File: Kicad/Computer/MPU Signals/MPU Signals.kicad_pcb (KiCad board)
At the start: 2 copper layers, 61 x 127 mm, 35 parts, among them IC1 FAN2558S38X, IC2 W65C816S6TQG-14, IC3 74LVC573AD,112, IC4 74LVC4245APW,118, IC5 74LVC04AD,118, IC6 74LVC32APW,118, IC7 74LVC1G08GV,125, IC8 74LVC11PW,112, J1 Conn_01x02_Male, J10 Conn_01x02_Male, J2 Conn_01x02_Male, J3 Conn_01x02_Male, J4 Conn_01x18_Male, J5 Conn_01x02_Male, J6 Conn_01x02_Male, J7 Conn_01x32_Male, J8 Conn_01x02_Male, J9 Conn_01x02_Male

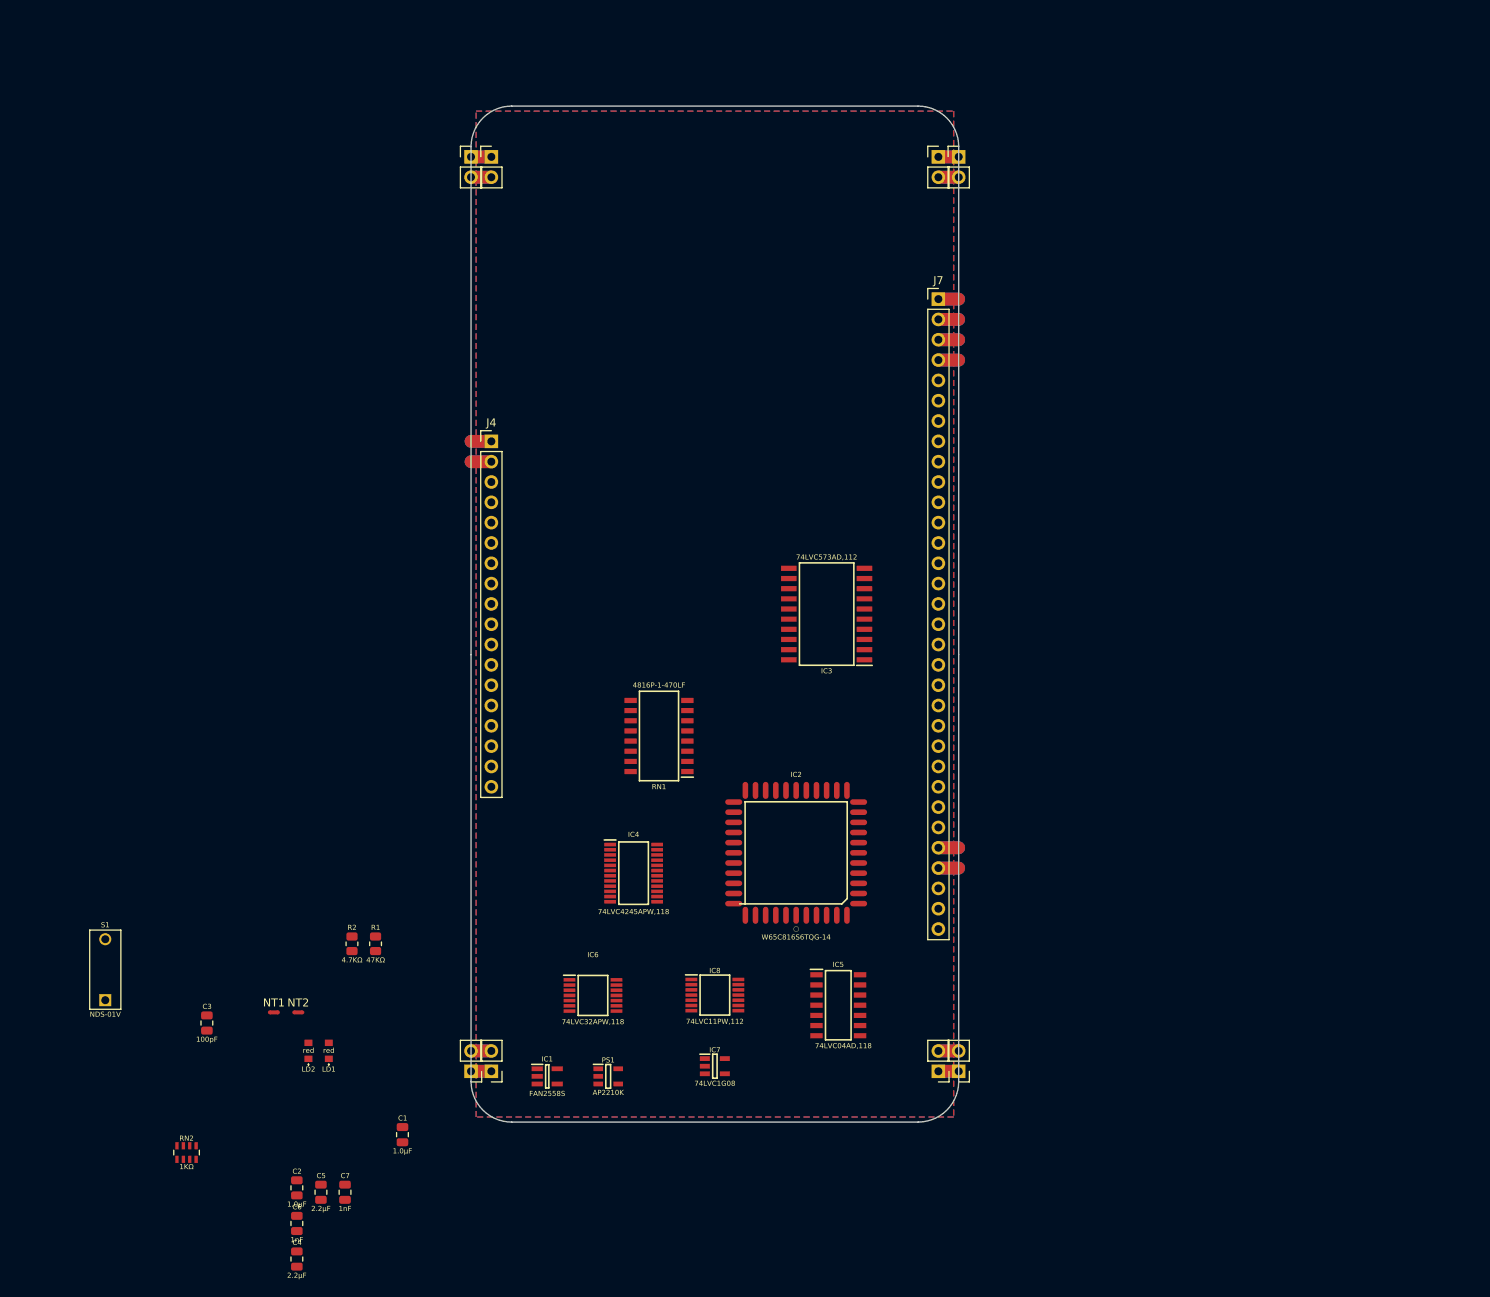
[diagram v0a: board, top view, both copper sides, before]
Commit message: Added Seven segment LED displays for CPU busses.
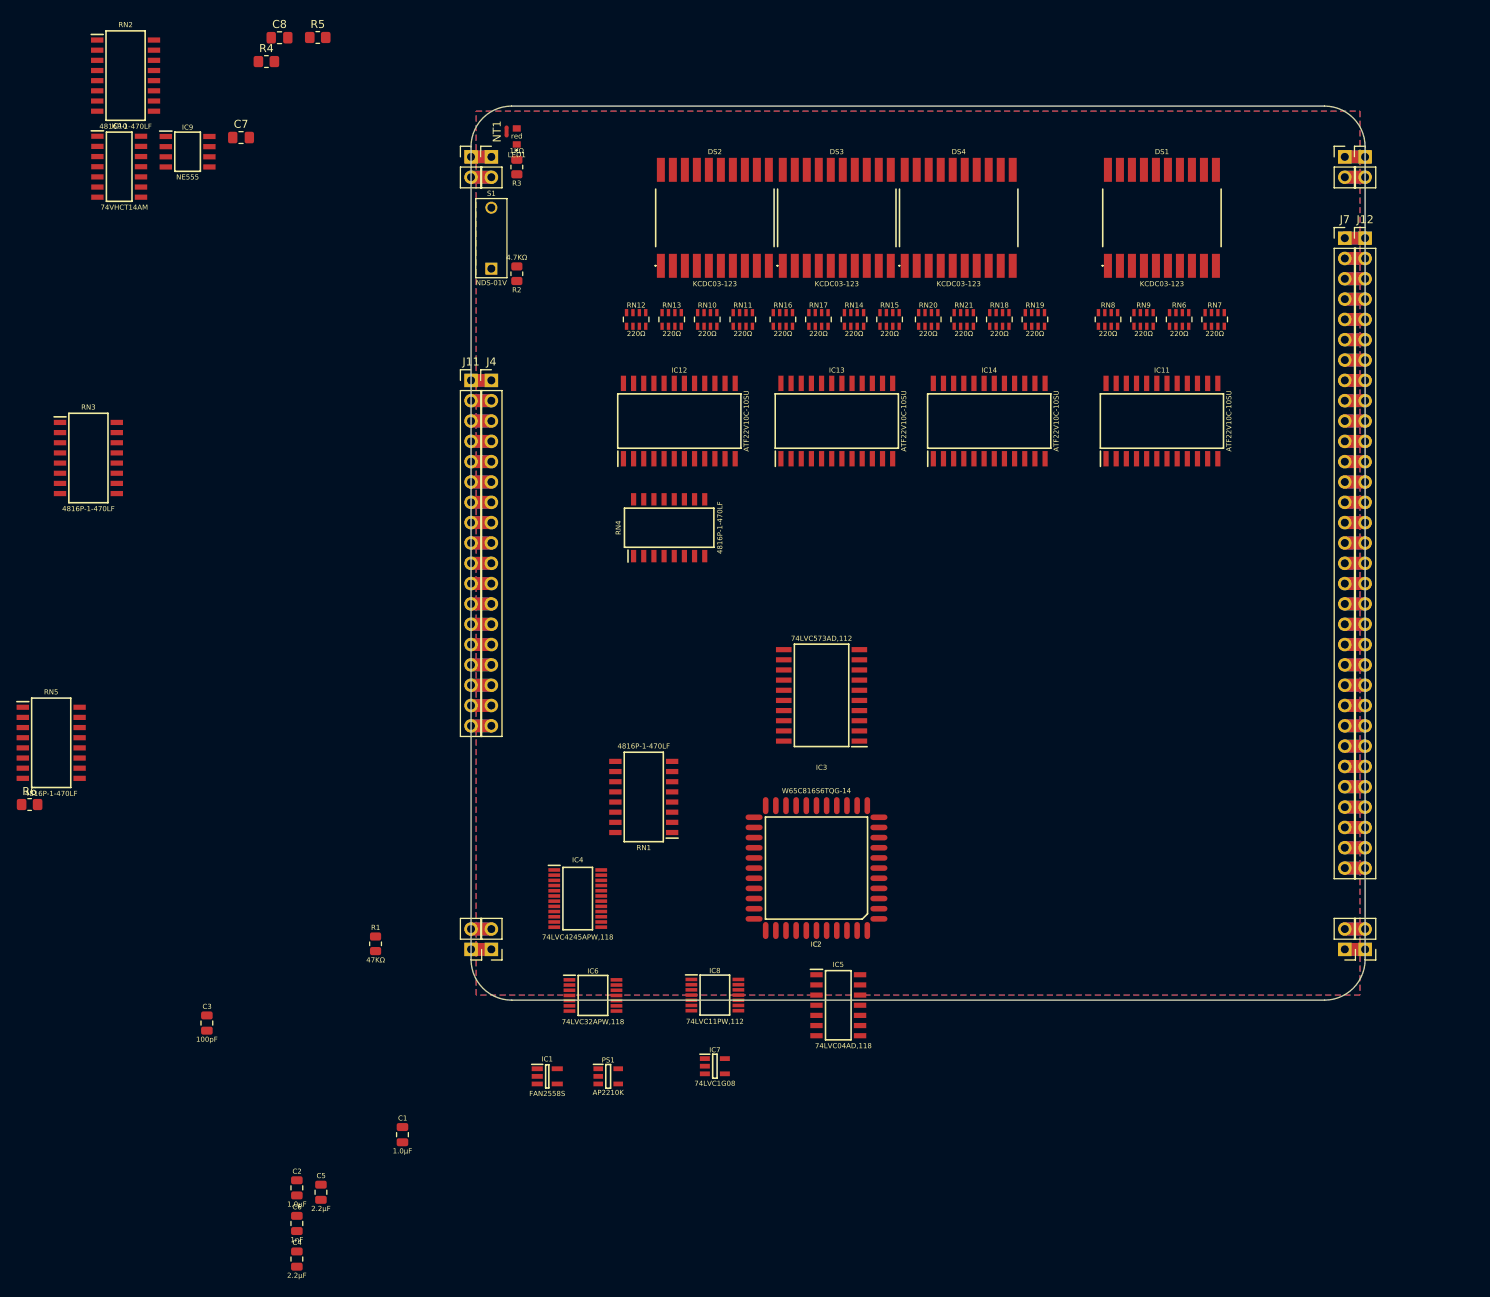
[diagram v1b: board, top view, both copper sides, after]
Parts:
- removed LD2: 150224SS73100, SamacSys_Parts:150224SS73100A
- removed NT2: NetTie_2, NetTie:NetTie-2_SMD_Pad0.5mm
- added C8: C_Small, Capacitor_SMD:C_0805_2012Metric_Pad1.18x1.45mm_HandSolder, F.Cu at (39.6, 41.0)
- added DS1: KCDC03-123, SamacSys_Parts:KCDC03123, F.Cu at (149.9, 63.5)
- added DS2: KCDC03-123, SamacSys_Parts:KCDC03123, F.Cu at (94.0, 63.5)
- added DS3: KCDC03-123, SamacSys_Parts:KCDC03123, F.Cu at (109.2, 63.5)
- added DS4: KCDC03-123, SamacSys_Parts:KCDC03123, F.Cu at (124.5, 63.5)
- added IC10: 74VHCT14AM, SamacSys_Parts:SOIC127P600X175-14N, F.Cu at (19.5, 57.1)
- added IC11: ATF22V10C-10SU, SamacSys_Parts:SOIC127P1032X265-24N, F.Cu at (149.9, 88.9)
- added IC12: ATF22V10C-10SU, SamacSys_Parts:SOIC127P1032X265-24N, F.Cu at (89.5, 88.9)
- added IC13: ATF22V10C-10SU, SamacSys_Parts:SOIC127P1032X265-24N, F.Cu at (109.2, 88.9)
- added IC14: ATF22V10C-10SU, SamacSys_Parts:SOIC127P1032X265-24N, F.Cu at (128.3, 88.9)
- added IC9: NE555DRG4, SamacSys_Parts:SOIC127P600X175-8N, F.Cu at (28.1, 55.2)
- added J11: Conn_01x18_Male, Connector_PinHeader_2.54mm:PinHeader_1x18_P2.54mm_Vertical, F.Cu at (63.5, 83.8)
- added J12: Conn_01x32_Male, Connector_PinHeader_2.54mm:PinHeader_1x32_P2.54mm_Vertical, F.Cu at (175.3, 66.0)
- added R3: R_0805, SamacSys_Parts:R_0805, F.Cu at (69.2, 57.1)
- added R4: R_Small, Resistor_SMD:R_0805_2012Metric_Pad1.20x1.40mm_HandSolder, F.Cu at (37.9, 44.0)
- added R5: R_Small, Resistor_SMD:R_0805_2012Metric_Pad1.20x1.40mm_HandSolder, F.Cu at (44.3, 41.0)
- added R6: R_Small, Resistor_SMD:R_0805_2012Metric_Pad1.20x1.40mm_HandSolder, F.Cu at (8.32, 136.8)
- added RN10: CAY16-221J4LF, SamacSys_Parts:CAY1647R0F4LF, F.Cu at (93.0, 76.2)
- added RN11: CAY16-221J4LF, SamacSys_Parts:CAY1647R0F4LF, F.Cu at (97.5, 76.2)
- added RN12: CAY16-221J4LF, SamacSys_Parts:CAY1647R0F4LF, F.Cu at (84.1, 76.2)
- added RN13: CAY16-221J4LF, SamacSys_Parts:CAY1647R0F4LF, F.Cu at (88.6, 76.2)
- added RN14: CAY16-221J4LF, SamacSys_Parts:CAY1647R0F4LF, F.Cu at (111.4, 76.2)
- added RN15: CAY16-221J4LF, SamacSys_Parts:CAY1647R0F4LF, F.Cu at (115.8, 76.2)
- added RN16: CAY16-221J4LF, SamacSys_Parts:CAY1647R0F4LF, F.Cu at (102.5, 76.2)
- added RN17: CAY16-221J4LF, SamacSys_Parts:CAY1647R0F4LF, F.Cu at (106.9, 76.2)
- added RN18: CAY16-221J4LF, SamacSys_Parts:CAY1647R0F4LF, F.Cu at (129.5, 76.2)
- added RN19: CAY16-221J4LF, SamacSys_Parts:CAY1647R0F4LF, F.Cu at (134.0, 76.2)
- added RN20: CAY16-221J4LF, SamacSys_Parts:CAY1647R0F4LF, F.Cu at (120.7, 76.2)
- added RN21: CAY16-221J4LF, SamacSys_Parts:CAY1647R0F4LF, F.Cu at (125.1, 76.2)
- added RN3: 4816P-1-470LF, SamacSys_Parts:SOIC127P762X240-16N, F.Cu at (15.7, 93.5)
- added RN4: 4816P-1-470LF, SamacSys_Parts:SOIC127P762X240-16N, F.Cu at (88.3, 102.2)
- added RN5: 4816P-1-470LF, SamacSys_Parts:SOIC127P762X240-16N, F.Cu at (11.0, 129.1)
- added RN6: CAY16-221J4LF, SamacSys_Parts:CAY1647R0F4LF, F.Cu at (152.0, 76.2)
- added RN7: CAY16-221J4LF, SamacSys_Parts:CAY1647R0F4LF, F.Cu at (156.5, 76.2)
- added RN8: CAY16-221J4LF, SamacSys_Parts:CAY1647R0F4LF, F.Cu at (143.1, 76.2)
- added RN9: CAY16-221J4LF, SamacSys_Parts:CAY1647R0F4LF, F.Cu at (147.6, 76.2)
- C7: value C_0805 -> C_Small; footprint SamacSys_Parts:C_0805 -> Capacitor_SMD:C_0805_2012Metric_Pad1.18x1.45mm_HandSolder
- RN2: value CAY16-102J4LF -> 4816P-1-470LF; footprint SamacSys_Parts:CAY16-J4 -> SamacSys_Parts:SOIC127P762X240-16N
- moved RN2 134.8 mm to (20.3, 45.7)
- moved C7 132.5 mm to (34.8, 53.5)
- moved LED1 116.7 mm to (69.2, 53.3)
- moved NT1 113.9 mm to (67.9, 52.7), turned to 90 degrees
- moved S1 103.4 mm to (66.0, 69.8)
- moved R2 86.3 mm to (69.2, 70.5), turned to 180 degrees
- moved J10 53.0 mm to (175.3, 154.9)
- moved J8 53.0 mm to (172.7, 154.9)
- moved J7 51.4 mm to (172.7, 66.0)
- moved J6 50.8 mm to (172.7, 55.9)
- moved J9 50.8 mm to (175.3, 55.9)
- moved J2 15.2 mm to (63.5, 154.9)
- moved J5 15.2 mm to (66.0, 154.9)
- moved IC3 10.2 mm to (107.3, 123.2)
- moved RN1 7.85 mm to (85.1, 135.9)
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- renumbered LD1 to LED1
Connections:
- net /LED Enable renamed /~{LED Enable}
- C7 pad 1: /5V -> Net-(C7-Pad1)
- IC4 pad 1: /5V -> unconnected-(IC4-Pad1)
- LED1 pad 1: Net-(LD1-Pad1) -> Net-(LED1-Pad1)
- RN2 pad 1: GND -> /A0
- RN2 pad 2: unconnected-(RN2-Pad2) -> /A1
- RN2 pad 3: unconnected-(RN2-Pad3) -> /A2
- RN2 pad 4: GND -> /A3
- RN2 pad 5: Net-(LD2-Pad1) -> /A4
- RN2 pad 6: unconnected-(RN2-Pad6) -> /A5
- RN2 pad 7: unconnected-(RN2-Pad7) -> /A6
- RN2 pad 8: Net-(LD1-Pad1) -> /A7
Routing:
- net /~{NMI}: track 0.00 -> 5.08 mm
- net /~{IRQ}: track 0.00 -> 5.08 mm
- net /~{Data Transmit}: track 0.00 -> 5.08 mm
- net /~{Clock Enable}: track 0.00 -> 5.08 mm
- net /Write Selector: track 0.00 -> 5.08 mm
- net /Read Selector: track 0.00 -> 5.08 mm
- net /RDY: track 0.00 -> 5.08 mm
- net /D7: track 0.00 -> 5.08 mm
- net /D6: track 0.00 -> 5.08 mm
- net /D5: track 0.00 -> 5.08 mm
- net /D4: track 0.00 -> 5.08 mm
- net /D3: track 0.00 -> 5.08 mm
- net /D2: track 0.00 -> 5.08 mm
- net /D1: track 0.00 -> 5.08 mm
- net /D0: track 0.00 -> 5.08 mm
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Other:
- board size 61 x 127 mm -> 111.8 x 111.8 mm

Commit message: MPU Signals.
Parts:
- removed RN2, RN4: 4816P-1-470LF, SamacSys_Parts:SOIC127P762X240-16N
- added J13: Conn_01x08_Male, Connector_PinHeader_2.54mm:PinHeader_1x12_P2.54mm_Vertical, B.Cu at (143.5, 77.5)
- added J14: Conn_01x12_Male, Connector_PinHeader_2.54mm:PinHeader_1x12_P2.54mm_Vertical, B.Cu at (143.5, 74.9)
- added J15: Conn_01x16_Male, Connector_PinHeader_2.54mm:PinHeader_1x12_P2.54mm_Vertical, B.Cu at (143.5, 133.3)
- added J16: Conn_01x12_Male, Connector_PinHeader_2.54mm:PinHeader_1x12_P2.54mm_Vertical, B.Cu at (143.5, 135.9)
- added J17: Conn_02x05_Counter_Clockwise, SamacSys_Parts:Pin_Socket_1.27mm 2x05, F.Cu at (135.9, 78.7)
- added J18: Conn_02x05_Counter_Clockwise, SamacSys_Parts:Pin_Header_1.27mm 2x05, B.Cu at (68.6, 78.7)
- added J19: SamacSys_Parts:Pin_Header_1.27mm 2x05, SamacSys_Parts:Pin_Header_1.27mm 2x05, B.Cu at (68.6, 130.8)
- added J20: Conn_02x05_Counter_Clockwise, SamacSys_Parts:Pin_Socket_1.27mm 2x05, F.Cu at (135.9, 130.8)
- added J21: SamacSys_Parts:Pin_Header_1.27mm 2x05, SamacSys_Parts:Pin_Header_1.27mm 2x05, B.Cu at (111.8, 78.7)
- added J22: Conn_02x05_Counter_Clockwise, SamacSys_Parts:Pin_Socket_1.27mm 2x05, F.Cu at (179.1, 78.7)
- added J23: SamacSys_Parts:Pin_Header_1.27mm 2x05, SamacSys_Parts:Pin_Header_1.27mm 2x05, B.Cu at (111.8, 130.8)
- added J24: Conn_02x05_Counter_Clockwise, SamacSys_Parts:Pin_Socket_1.27mm 2x05, F.Cu at (179.1, 130.8)
- C6, C7, C8, IC11, IC12, IC13, IC14, IC9, J1, J10, J2, J3, J5, J6, J8, J9, NT1, R3, R4, R5, R6: moved to B.Cu
- IC10: value 74VHCT14AM -> 74LVC1G17GV,125; footprint SamacSys_Parts:SOIC127P600X175-14N -> SamacSys_Parts:SOT95P275X110-5N; moved to B.Cu
- J11, J4: value Conn_01x18_Male -> Conn_01x10_Male; footprint Connector_PinHeader_2.54mm:PinHeader_1x18_P2.54mm_Vertical -> Connector_PinHeader_2.54mm:PinHeader_1x10_P2.54mm_Vertical; moved to B.Cu
- J12, J7: value Conn_01x32_Male -> Conn_01x16_Male; footprint Connector_PinHeader_2.54mm:PinHeader_1x32_P2.54mm_Vertical -> Connector_PinHeader_2.54mm:PinHeader_1x16_P2.54mm_Vertical; moved to B.Cu
- moved RN3 157.1 mm to (172.7, 95.2), turned to 90 degrees
- moved RN5 154.8 mm to (160.0, 87.0), turned to -90 degrees
- moved C4 151.9 mm to (147.3, 84.5), turned to 90 degrees
- moved C3 138.2 mm to (148.0, 91.4), turned to 90 degrees
- moved C5 137.7 mm to (138.4, 84.5), turned to 90 degrees
- moved C2 134.8 mm to (135.3, 87.6)
- moved C1 127.1 mm to (144.1, 87.6)
- moved C6 120.0 mm to (110.3, 90.8), turned to -90 degrees
- moved R6 107.8 mm to (101.1, 81.9)
- moved R1 107.2 mm to (138.4, 91.4), turned to 90 degrees
- moved PS1 107.0 mm to (148.0, 87.6)
- moved IC1 105.8 mm to (138.4, 87.6)
- moved IC10 95.5 mm to (110.0, 87.6)
- moved IC4 95.0 mm to (157.5, 98.4), turned to -90 degrees
- moved R4 87.0 mm to (113.2, 87.6), turned to 90 degrees
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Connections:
- net /Address High Display/Digit 0 C Seg renamed /High Address Display/Digit 0 C Seg
- net /Address High Display/Digit 0 D Seg renamed /High Address Display/Digit 0 D Seg
- net /Address High Display/Digit 0 E Seg renamed /High Address Display/Digit 0 E Seg
- net /Address High Display/Digit L0 Cathode renamed /High Address Display/Digit L0 Cathode
- net /Address High Display/Digit R0 Cathode renamed /High Address Display/Digit R0 Cathode
- net /Address Low Display/Digit 0 C Seg renamed /Low Address Display/Digit 0 C Seg
- net /Address Low Display/Digit 0 D Seg renamed /Low Address Display/Digit 0 D Seg
- net /Address Low Display/Digit 0 E Seg renamed /Low Address Display/Digit 0 E Seg
- net /Address Low Display/Digit L0 Cathode renamed /Low Address Display/Digit L0 Cathode
- net /Address Low Display/Digit R0 Cathode renamed /Low Address Display/Digit R0 Cathode
- net /BA Display/Digit 0 C Seg renamed /Bank Address Display/Digit 0 C Seg
- net /BA Display/Digit 0 D Seg renamed /Bank Address Display/Digit 0 D Seg
- net /BA Display/Digit 0 E Seg renamed /Bank Address Display/Digit 0 E Seg
- net /BA Display/Digit L0 Cathode renamed /Bank Address Display/Digit L0 Cathode
- net /BA Display/Digit R0 Cathode renamed /Bank Address Display/Digit R0 Cathode
- C6 pad 1: /5V -> /3.8V_{TOP}
- C6 pad 2: GND -> /GND_{TOP}
- C7 pad 2: GND -> /GND_{TOP}
- C8 pad 2: GND -> /GND_{TOP}
- DS1 pad 10: GND -> /GND_{TOP}
- DS1 pad 5: GND -> /GND_{TOP}
- DS2 pad 10: GND -> /GND_{TOP}
- DS2 pad 5: GND -> /GND_{TOP}
- DS3 pad 10: GND -> /GND_{TOP}
- DS3 pad 5: GND -> /GND_{TOP}
- DS4 pad 10: GND -> /GND_{TOP}
- DS4 pad 5: GND -> /GND_{TOP}
- IC10 pad 1: Net-(IC10-Pad1) -> unconnected-(IC10-Pad1)
- IC10 pad 2: GND -> Net-(IC10-Pad2)
- IC10 pad 3: Net-(IC10-Pad3) -> /GND_{TOP}
- IC10 pad 4: unconnected-(IC10-Pad4) -> Net-(IC10-Pad4)
- IC10 pad 5: Net-(IC10-Pad3) -> /3.8V_{TOP}
- IC11 pad 12: GND -> /GND_{TOP}
- IC11 pad 13: GND -> /GND_{TOP}
- IC11 pad 2: /LD0 -> /LD0_{TOP}
- IC11 pad 24: /5V -> /5V_{TOP}
- IC11 pad 3: /LD1 -> /LD1_{TOP}
- IC11 pad 4: /LD2 -> /LD2_{TOP}
- IC11 pad 5: /LD3 -> /LD3_{TOP}
- IC11 pad 6: /LD4 -> /LD4_{TOP}
- IC11 pad 7: /LD5 -> /LD5_{TOP}
- IC11 pad 8: /LD6 -> /LD6_{TOP}
- IC11 pad 9: /LD7 -> /LD7_{TOP}
- IC12 pad 12: GND -> /GND_{TOP}
- IC12 pad 13: GND -> /GND_{TOP}
- IC12 pad 16: /BA Display/Digit 0 B Seg -> /Bank Address Display/Digit 0 B Seg
- IC12 pad 17: /BA Display/Digit 0 A Seg -> /Bank Address Display/Digit 0 A Seg
- IC12 pad 19: /BA Display/Digit 0 F Seg -> /Bank Address Display/Digit 0 F Seg
- IC12 pad 2: /LBA0 -> /BA0_{TOP}
- IC12 pad 21: /BA Display/Digit 0 G Seg -> /Bank Address Display/Digit 0 G Seg
- IC12 pad 24: /5V -> /5V_{TOP}
- IC12 pad 3: /LBA1 -> /BA1_{TOP}
- IC12 pad 4: /LBA2 -> /BA2_{TOP}
- IC12 pad 5: /LBA3 -> /BA3_{TOP}
- IC12 pad 6: /LBA4 -> /BA4_{TOP}
- IC12 pad 7: /LBA5 -> /BA5_{TOP}
- IC12 pad 8: /LBA6 -> /BA6_{TOP}
- IC12 pad 9: /LBA7 -> /BA7_{TOP}
- IC13 pad 12: GND -> /GND_{TOP}
- IC13 pad 13: GND -> /GND_{TOP}
- IC13 pad 16: /Address High Display/Digit 0 B Seg -> /High Address Display/Digit 0 B Seg
- IC13 pad 17: /Address High Display/Digit 0 A Seg -> /High Address Display/Digit 0 A Seg
- IC13 pad 19: /Address High Display/Digit 0 F Seg -> /High Address Display/Digit 0 F Seg
- IC13 pad 2: /A8 -> /LA8_{TOP}
- IC13 pad 21: /Address High Display/Digit 0 G Seg -> /High Address Display/Digit 0 G Seg
- IC13 pad 24: /5V -> /5V_{TOP}
- IC13 pad 3: /A9 -> /LA9_{TOP}
- IC13 pad 4: /A10 -> /LA10_{TOP}
- IC13 pad 5: /A11 -> /LA11_{TOP}
- IC13 pad 6: /A12 -> /LA12_{TOP}
- IC13 pad 7: /A13 -> /LA13_{TOP}
- IC13 pad 8: /A14 -> /LA14_{TOP}
- IC13 pad 9: /A15 -> /LA15_{TOP}
- IC14 pad 12: GND -> /GND_{TOP}
- IC14 pad 13: GND -> /GND_{TOP}
- IC14 pad 16: /Address Low Display/Digit 0 B Seg -> /Low Address Display/Digit 0 B Seg
- IC14 pad 17: /Address Low Display/Digit 0 A Seg -> /Low Address Display/Digit 0 A Seg
- IC14 pad 19: /Address Low Display/Digit 0 F Seg -> /Low Address Display/Digit 0 F Seg
- IC14 pad 2: /A0 -> /A0_{TOP}
- IC14 pad 21: /Address Low Display/Digit 0 G Seg -> /Low Address Display/Digit 0 G Seg
- IC14 pad 24: /5V -> /5V_{TOP}
- IC14 pad 3: /A1 -> /A1_{TOP}
- IC14 pad 4: /A2 -> /A2_{TOP}
- IC14 pad 5: /A3 -> /A3_{TOP}
- IC14 pad 6: /A4 -> /A4_{TOP}
- IC14 pad 7: /A5 -> /A5_{TOP}
- IC14 pad 8: /A6 -> /A6_{TOP}
- IC14 pad 9: /A7 -> /A7_{TOP}
- IC9 pad 1: GND -> /GND_{TOP}
- IC9 pad 3: Net-(IC10-Pad1) -> Net-(IC10-Pad2)
- IC9 pad 4: /5V -> /5V_{TOP}
- IC9 pad 8: /5V -> /5V_{TOP}
- J1 pad 2: unconnected-(J1-Pad2) -> /Source 5V
- J11 pad 10: /D3 -> /~{Data Transmit}
- J11 pad 6: /D7 -> /Read Selector
- J11 pad 7: /D6 -> /Write Selector
- J11 pad 8: /D5 -> /~{Clock Enable}
- J11 pad 9: /D4 -> /Bank Latch
- J12 pad 1: /BA7 -> /A15
- J12 pad 10: /A14 -> /A6
- J12 pad 11: /A13 -> /A5
- J12 pad 12: /A12 -> /A4
- J12 pad 13: /A11 -> /A3
- J12 pad 14: /A10 -> /A2
- J12 pad 15: /A9 -> /A1
- J12 pad 16: /A8 -> /A0
- J12 pad 2: /BA6 -> /A14
- J12 pad 3: /BA5 -> /A13
- J12 pad 4: /BA4 -> /A12
- J12 pad 5: /BA3 -> /A11
- J12 pad 6: /BA2 -> /A10
- J12 pad 7: /BA1 -> /A9
- J12 pad 8: /BA0 -> /A8
- J12 pad 9: /A15 -> /A7
- J2 pad 2: /Source 5V -> unconnected-(J2-Pad2)
- J3 pad 2: unconnected-(J1-Pad2) -> /Source 5V
- J4 pad 10: /D3 -> /~{Data Transmit}
- J4 pad 6: /D7 -> /Read Selector
- J4 pad 7: /D6 -> /Write Selector
- J4 pad 8: /D5 -> /~{Clock Enable}
- J4 pad 9: /D4 -> /Bank Latch
- J5 pad 2: /Source 5V -> unconnected-(J2-Pad2)
- J7 pad 1: /BA7 -> /A15
- J7 pad 10: /A14 -> /A6
- J7 pad 11: /A13 -> /A5
- J7 pad 12: /A12 -> /A4
- J7 pad 13: /A11 -> /A3
- J7 pad 14: /A10 -> /A2
- J7 pad 15: /A9 -> /A1
- J7 pad 16: /A8 -> /A0
- J7 pad 2: /BA6 -> /A14
- J7 pad 3: /BA5 -> /A13
- J7 pad 4: /BA4 -> /A12
- J7 pad 5: /BA3 -> /A11
- J7 pad 6: /BA2 -> /A10
- J7 pad 7: /BA1 -> /A9
- J7 pad 8: /BA0 -> /A8
- J7 pad 9: /A15 -> /A7
- NT1 pad 1: /5V -> /5V_{TOP}
- R2 pad 2: /5V -> /5V_{TOP}
- R3 pad 2: GND -> /GND_{TOP}
- R4 pad 2: Net-(IC10-Pad13) -> Net-(IC10-Pad4)
- R6 pad 2: /5V -> /5V_{TOP}
- RN12 pad 1: Net-(DS2-Pad20) -> Net-(DS2-Pad16)
- RN12 pad 2: Net-(DS2-Pad19) -> Net-(DS2-Pad17)
- RN12 pad 3: Net-(DS2-Pad17) -> Net-(DS2-Pad19)
- RN12 pad 4: Net-(DS2-Pad16) -> Net-(DS2-Pad20)
- RN12 pad 5: /BA Display/Digit 0 B Seg -> /Bank Address Display/Digit 0 G Seg
- RN12 pad 6: /BA Display/Digit 0 A Seg -> /Bank Address Display/Digit 0 F Seg
- RN12 pad 7: /BA Display/Digit 0 F Seg -> /Bank Address Display/Digit 0 A Seg
- RN12 pad 8: /BA Display/Digit 0 G Seg -> /Bank Address Display/Digit 0 B Seg
- RN13 pad 1: Net-(DS2-Pad15) -> Net-(DS2-Pad11)
- RN13 pad 2: Net-(DS2-Pad14) -> Net-(DS2-Pad12)
- RN13 pad 3: Net-(DS2-Pad12) -> Net-(DS2-Pad14)
- RN13 pad 4: Net-(DS2-Pad11) -> Net-(DS2-Pad15)
- RN13 pad 5: /BA Display/Digit 0 B Seg -> /Bank Address Display/Digit 0 G Seg
- RN13 pad 6: /BA Display/Digit 0 A Seg -> /Bank Address Display/Digit 0 F Seg
- RN13 pad 7: /BA Display/Digit 0 F Seg -> /Bank Address Display/Digit 0 A Seg
- RN13 pad 8: /BA Display/Digit 0 G Seg -> /Bank Address Display/Digit 0 B Seg
- RN16 pad 1: Net-(DS3-Pad20) -> Net-(DS3-Pad16)
- RN16 pad 2: Net-(DS3-Pad19) -> Net-(DS3-Pad17)
- RN16 pad 3: Net-(DS3-Pad17) -> Net-(DS3-Pad19)
- RN16 pad 4: Net-(DS3-Pad16) -> Net-(DS3-Pad20)
- RN16 pad 5: /Address High Display/Digit 0 B Seg -> /High Address Display/Digit 0 G Seg
- RN16 pad 6: /Address High Display/Digit 0 A Seg -> /High Address Display/Digit 0 F Seg
- RN16 pad 7: /Address High Display/Digit 0 F Seg -> /High Address Display/Digit 0 A Seg
- RN16 pad 8: /Address High Display/Digit 0 G Seg -> /High Address Display/Digit 0 B Seg
- RN17 pad 1: Net-(DS3-Pad15) -> Net-(DS3-Pad11)
- RN17 pad 2: Net-(DS3-Pad14) -> Net-(DS3-Pad12)
- RN17 pad 3: Net-(DS3-Pad12) -> Net-(DS3-Pad14)
- RN17 pad 4: Net-(DS3-Pad11) -> Net-(DS3-Pad15)
- RN17 pad 5: /Address High Display/Digit 0 B Seg -> /High Address Display/Digit 0 G Seg
- RN17 pad 6: /Address High Display/Digit 0 A Seg -> /High Address Display/Digit 0 F Seg
- RN17 pad 7: /Address High Display/Digit 0 F Seg -> /High Address Display/Digit 0 A Seg
- RN17 pad 8: /Address High Display/Digit 0 G Seg -> /High Address Display/Digit 0 B Seg
- RN20 pad 1: Net-(DS4-Pad20) -> Net-(DS4-Pad16)
- RN20 pad 2: Net-(DS4-Pad19) -> Net-(DS4-Pad17)
- RN20 pad 3: Net-(DS4-Pad17) -> Net-(DS4-Pad19)
- RN20 pad 4: Net-(DS4-Pad16) -> Net-(DS4-Pad20)
- RN20 pad 5: /Address Low Display/Digit 0 B Seg -> /Low Address Display/Digit 0 G Seg
- RN20 pad 6: /Address Low Display/Digit 0 A Seg -> /Low Address Display/Digit 0 F Seg
- RN20 pad 7: /Address Low Display/Digit 0 F Seg -> /Low Address Display/Digit 0 A Seg
- RN20 pad 8: /Address Low Display/Digit 0 G Seg -> /Low Address Display/Digit 0 B Seg
- RN21 pad 1: Net-(DS4-Pad15) -> Net-(DS4-Pad11)
- RN21 pad 2: Net-(DS4-Pad14) -> Net-(DS4-Pad12)
- RN21 pad 3: Net-(DS4-Pad12) -> Net-(DS4-Pad14)
- RN21 pad 4: Net-(DS4-Pad11) -> Net-(DS4-Pad15)
- RN21 pad 5: /Address Low Display/Digit 0 B Seg -> /Low Address Display/Digit 0 G Seg
- RN21 pad 6: /Address Low Display/Digit 0 A Seg -> /Low Address Display/Digit 0 F Seg
- RN21 pad 7: /Address Low Display/Digit 0 F Seg -> /Low Address Display/Digit 0 A Seg
- RN21 pad 8: /Address Low Display/Digit 0 G Seg -> /Low Address Display/Digit 0 B Seg
- RN3 pad 1: /A8 -> /A15
- RN3 pad 10: /LA14 -> /LA9
- RN3 pad 11: /LA13 -> /LA10
- RN3 pad 12: /LA12 -> /LA11
- RN3 pad 13: /LA11 -> /LA12
- RN3 pad 14: /LA10 -> /LA13
- RN3 pad 15: /LA9 -> /LA14
- RN3 pad 16: /LA8 -> /LA15
- RN3 pad 2: /A9 -> /A14
- RN3 pad 3: /A10 -> /A13
- RN3 pad 4: /A11 -> /A12
- RN3 pad 5: /A12 -> /A11
- RN3 pad 6: /A13 -> /A10
- RN3 pad 7: /A14 -> /A9
- RN3 pad 8: /A15 -> /A8
- RN3 pad 9: /LA15 -> /LA8
- RN8 pad 1: Net-(DS1-Pad20) -> Net-(DS1-Pad16)
- RN8 pad 2: Net-(DS1-Pad19) -> Net-(DS1-Pad17)
- RN8 pad 3: Net-(DS1-Pad17) -> Net-(DS1-Pad19)
- RN8 pad 4: Net-(DS1-Pad16) -> Net-(DS1-Pad20)
- RN8 pad 5: /Data Display/Digit 0 B Seg -> /Data Display/Digit 0 G Seg
- RN8 pad 6: /Data Display/Digit 0 A Seg -> /Data Display/Digit 0 F Seg
- RN8 pad 7: /Data Display/Digit 0 F Seg -> /Data Display/Digit 0 A Seg
- RN8 pad 8: /Data Display/Digit 0 G Seg -> /Data Display/Digit 0 B Seg
- RN9 pad 1: Net-(DS1-Pad15) -> Net-(DS1-Pad11)
- RN9 pad 2: Net-(DS1-Pad14) -> Net-(DS1-Pad12)
- RN9 pad 3: Net-(DS1-Pad12) -> Net-(DS1-Pad14)
- RN9 pad 4: Net-(DS1-Pad11) -> Net-(DS1-Pad15)
- RN9 pad 5: /Data Display/Digit 0 B Seg -> /Data Display/Digit 0 G Seg
- RN9 pad 6: /Data Display/Digit 0 A Seg -> /Data Display/Digit 0 F Seg
- RN9 pad 7: /Data Display/Digit 0 F Seg -> /Data Display/Digit 0 A Seg
- RN9 pad 8: /Data Display/Digit 0 G Seg -> /Data Display/Digit 0 B Seg
- S1 pad 2: GND -> /GND_{TOP}
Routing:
- net unconnected-(J1-Pad2): track 5.08 -> 0.00 mm
- net unconnected-(J2-Pad2): track 0.00 -> 5.08 mm
- removed copper zone on B.Cu, net (none)
- removed copper zone on F.Cu, net (none)
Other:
- board size 111.8 x 111.8 mm -> 128.3 x 61 mm
